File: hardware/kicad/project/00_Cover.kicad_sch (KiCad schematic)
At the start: 0 parts

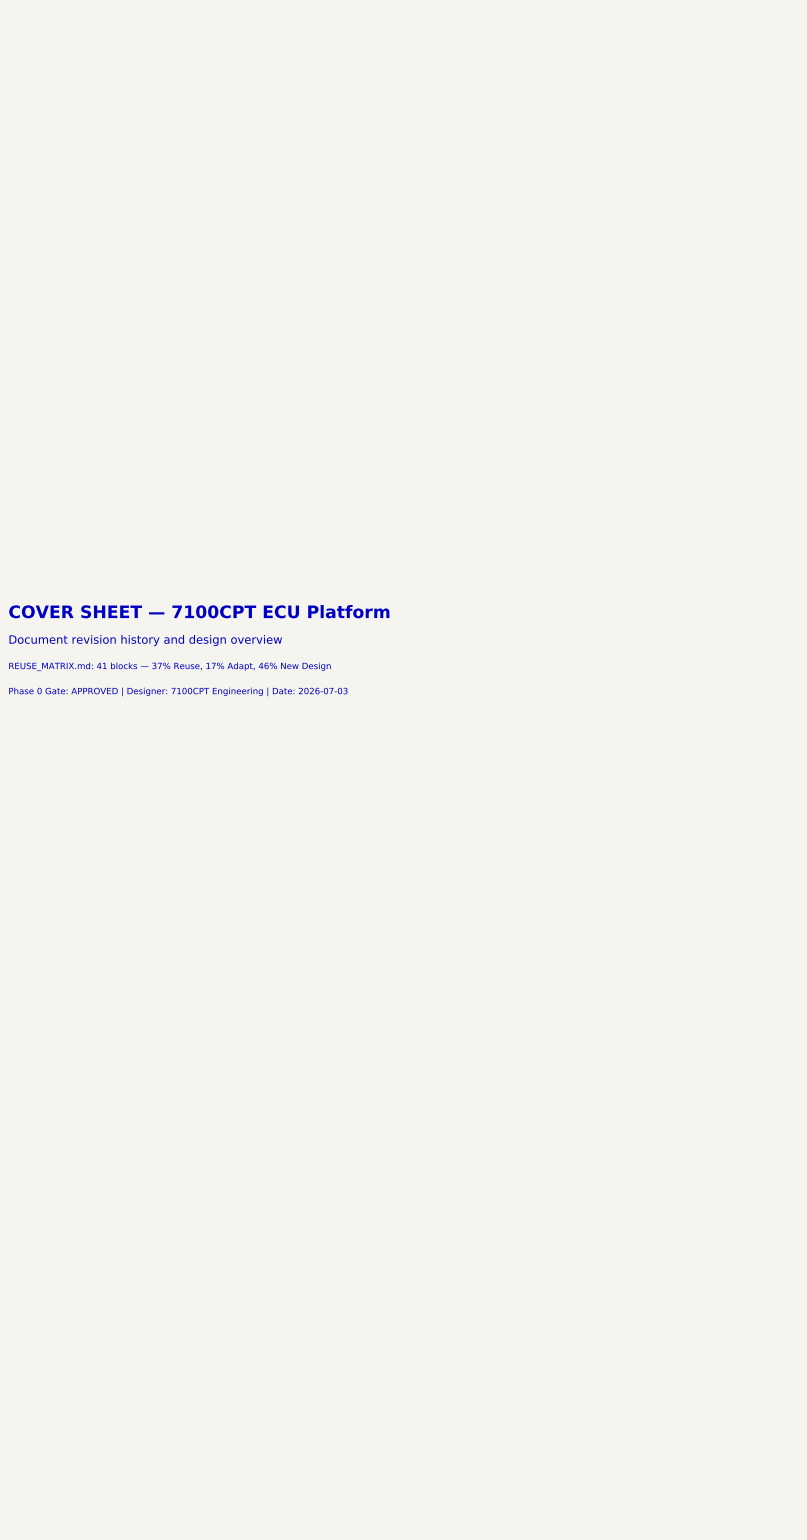
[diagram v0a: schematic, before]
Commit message: feat(hardware): TB-HW-002 — populate all 12 schematic sheets with components
Populated 235 component symbols across all 12 KiCad schematic sheets:
- 01_Power: Reverse polarity, TVS (SMCJ33A), buck (LMR33630), LDO (TPS7A1633), VREF (REF5050) — 30 symbols
- 02_MCU: S32K344 (6 units), clock (40MHz+32kHz), decoupling, reset, boot config, LEDs — 30 symbols
- 03_CAN: 4x TJA1043 with CM chokes (ACT45B-510), split termination, bus filter caps — 36 symbols
- 04_USB: Molex USB-C, TPD2EUSB30 ESD, CC resistors, eFuse, Ethernet PHY footprint — 9 symbols
- 05_Inputs: 8 analog channels (RC+clamp), 2x CJ125 WBO2, 2x TLE2072 knock amps — 50 symbols
- 06_Injectors: TLE8888-2QK (8-ch P&H), flyback diodes, current sense — 14 symbols
- 07_Ignition: 6x ISL9V3040S3 IGBTs with gate resistors (100R), pull-downs (10k) — 24 symbols
- 08_Outputs: DRV8873 ETC H-bridge, TLE8110ED low-side (boost+relays), BTS4140N tach — 12 symbols
- 09_Protection: TPS3850G33 watchdog, safe-state FET, ESD diodes (PESD5V0) — 14 symbols
- 10_Connectors: 42-pin Deutsch DTM (2 units), 2x CAN 4-pin, diagnostic 4-pin — 5 symbols
- 11_Programming: TC2050 SWD, 8 test points, production security notes — 11 symbols
- 00_Cover: Block diagram, BOM summary, spec references, revision history

Symbol library: 18 custom symbols with complete pin assignments
Components from COMPONENT_SELECTION.md r0.1
42-pin connector per INTERFACE_SPECIFICATION.md (authority)
All MCU pins per MCU_SELECTION.md pin allocation
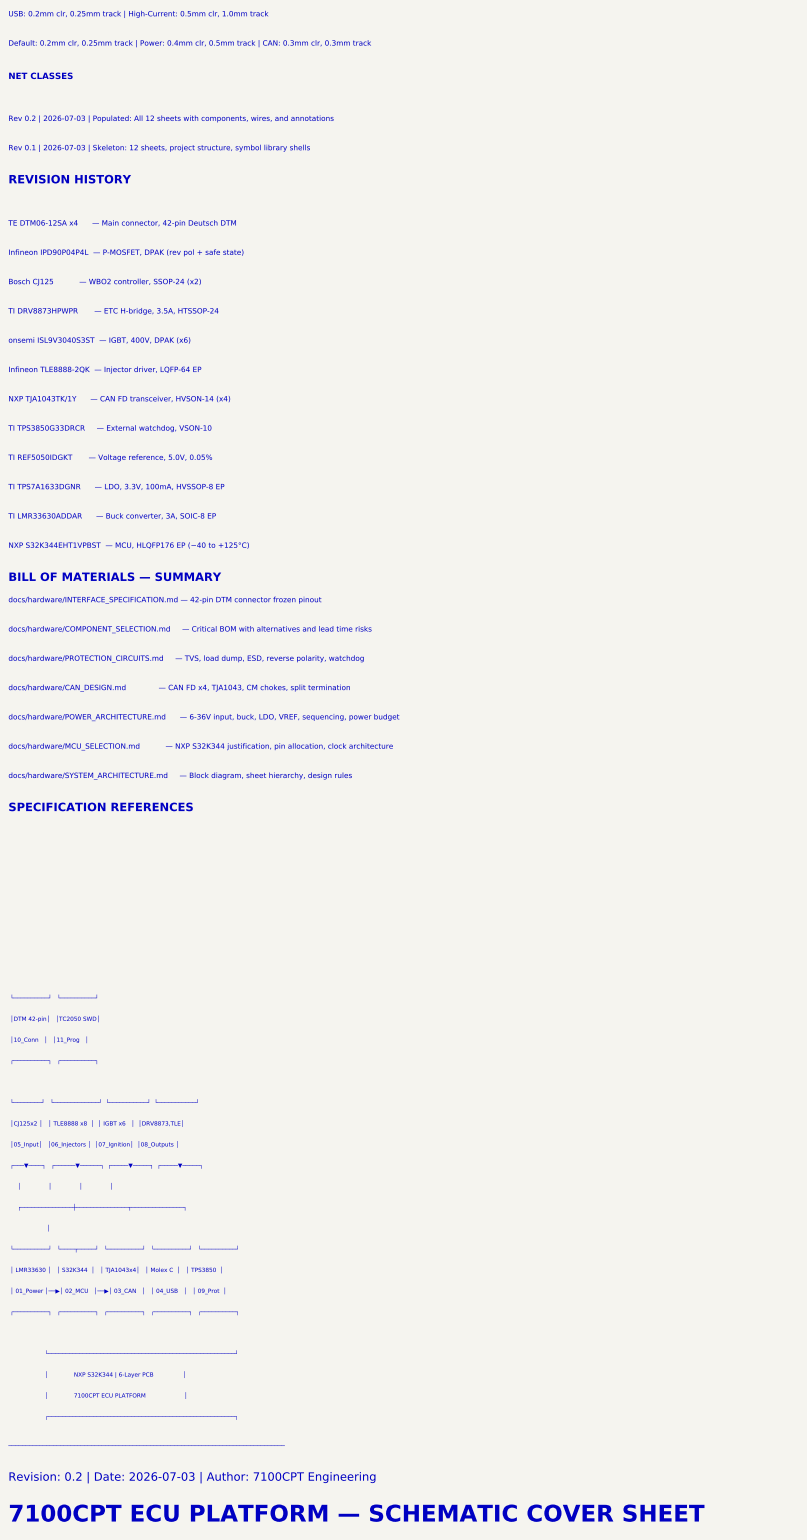
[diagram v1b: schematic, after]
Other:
- note added: "7100CPT ECU PLATFORM — SCHEMATIC COVER SHEET"
- note added: "BILL OF MATERIALS — SUMMARY"
- note added: "Bosch CJ125 — WBO2 controller, SSOP-24 (x2)"
- note added: "Default: 0.2mm clr, 0.25mm track | Power: 0.4mm clr, 0.5mm track | CAN: 0.3mm clr, 0.3mm track"
- note added: "Infineon IPD90P04P4L — P-MOSFET, DPAK (rev pol + safe state)"
- note added: "Infineon TLE8888-2QK — Injector driver, LQFP-64 EP"
- note added: "NET CLASSES"
- note added: "NXP S32K344EHT1VPBST — MCU, HLQFP176 EP (−40 to +125°C)"
- note added: "NXP TJA1043TK/1Y — CAN FD transceiver, HVSON-14 (x4)"
- note added: "REVISION HISTORY"
- note added: "Rev 0.1 | 2026-07-03 | Skeleton: 12 sheets, project structure, symbol library shells"
- note added: "Rev 0.2 | 2026-07-03 | Populated: All 12 sheets with components, wires, and annotations"
- note added: "Revision: 0.2 | Date: 2026-07-03 | Author: 7100CPT Engineering"
- note added: "SPECIFICATION REFERENCES"
- note added: "TE DTM06-12SA x4 — Main connector, 42-pin Deutsch DTM"
- note added: "TI DRV8873HPWPR — ETC H-bridge, 3.5A, HTSSOP-24"
- note added: "TI LMR33630ADDAR — Buck converter, 3A, SOIC-8 EP"
- note added: "TI REF5050IDGKT — Voltage reference, 5.0V, 0.05%"
- note added: "TI TPS3850G33DRCR — External watchdog, VSON-10"
- note added: "TI TPS7A1633DGNR — LDO, 3.3V, 100mA, HVSSOP-8 EP"
- note added: "USB: 0.2mm clr, 0.25mm track | High-Current: 0.5mm clr, 1.0mm track"
- note added: "docs/hardware/CAN_DESIGN.md — CAN FD x4, TJA1043, CM chokes, split termination"
- note added: "docs/hardware/COMPONENT_SELECTION.md — Critical BOM with alternatives and lead time risks"
- note added: "docs/hardware/INTERFACE_SPECIFICATION.md — 42-pin DTM connector frozen pinout"
- note added: "docs/hardware/MCU_SELECTION.md — NXP S32K344 justification, pin allocation, clock architecture"
- note added: "docs/hardware/POWER_ARCHITECTURE.md — 6-36V input, buck, LDO, VREF, sequencing, power budget"
- note added: "docs/hardware/PROTECTION_CIRCUITS.md — TVS, load dump, ESD, reverse polarity, watchdog"
- note added: "docs/hardware/SYSTEM_ARCHITECTURE.md — Block diagram, sheet hierarchy, design rules"
- note added: "onsemi ISL9V3040S3ST — IGBT, 400V, DPAK (x6)"
- note added: "────────────────────────────────────────────────────────────────────────────────"
- note added: "│"
- note added: "│ 01_Power │──▶│ 02_MCU │──▶│ 03_CAN │ │ 04_USB │ │ 09_Prot │"
- note added: "│ 7100CPT ECU PLATFORM │"
- note added: "│ LMR33630 │ │ S32K344 │ │ TJA1043x4│ │ Molex C │ │ TPS3850 │"
- note added: "│ NXP S32K344 | 6-Layer PCB │"
- note added: "│ │ │ │"
- note added: "│05_Input│ │06_Injectors │ │07_Ignition│ │08_Outputs │"
- note added: "│10_Conn │ │11_Prog │"
- note added: "│CJ125x2 │ │ TLE8888 x8 │ │ IGBT x6 │ │DRV8873,TLE│"
- note added: "│DTM 42-pin│ │TC2050 SWD│"
- note added: "┌──────────────────────────────────────────────────────┐"
- note added: "┌───────────────┼───────────────┬───────────────┐"
- note added: "┌──────────┐ ┌──────────┐"
- note added: "┌──────────┐ ┌──────────┐ ┌──────────┐ ┌──────────┐ ┌──────────┐"
- note added: "┌───▼────┐ ┌──────▼──────┐ ┌─────▼─────┐ ┌─────▼─────┐"
- note added: "└──────────────────────────────────────────────────────┘"
- note added: "└──────────┘ └──────────┘"
- note added: "└──────────┘ └────┬─────┘ └──────────┘ └──────────┘ └──────────┘"
- note added: "└────────┘ └─────────────┘ └───────────┘ └───────────┘"
- note removed: "COVER SHEET — 7100CPT ECU Platform"
- note removed: "Document revision history and design overview"
- note removed: "Phase 0 Gate: APPROVED | Designer: 7100CPT Engineering | Date: 2026-07-03"
- note removed: "REUSE_MATRIX.md: 41 blocks — 37% Reuse, 17% Adapt, 46% New Design"
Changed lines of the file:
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@@
-(kicad_sch (version 20240108) (generator "eeschema")
+(kicad_sch (version 20240108) (generator "7100CPT-schematic-gen")
   (paper "A3")
   (title_block
     (title "7100CPT ECU — Cover & Revision History")
     (date "2026-07-03")
-    (rev "0.1")
+    (rev "0.2")
     (company "${COMPANY}")
-    (comment 1 "Revision history, block diagram, BOM summary, REUSE_MATRIX reference")
+    (comment 1 "Cover sheet, block diagram, BOM summary, REUSE_MATRIX reference")
     (comment 2 "NXP S32K344 | rusEFI Firmware | IPC Class 3")
     (comment 3 "High-Tg FR-4 (TG170+) | ENIG | 1.6 mm")
-    (comment 4 "REUSE_MATRIX.md — NXP Reference Following")
+    (comment 4 "Phase 0 Approved | REUSE_MATRIX gate passed")
     (comment 5 "-40C to +85C | IP67 Target | 6-Layer")
   )
   (symbol_instances)
-  (text "COVER SHEET — 7100CPT ECU Platform"
-    (at 25 24 0) (effects (font (size 3.0 3.0) bold) (justify left bottom)))
-  (text "Document revision history and design overview"
-    (at 25 30 0) (effects (font (size 2.0 2.0)) (justify left bottom)))
-  (text "REUSE_MATRIX.md: 41 blocks — 37% Reuse, 17% Adapt, 46% New Design"
-    (at 25 36 0) (effects (font (size 1.5 1.5)) (justify left bottom)))
-  (text "Phase 0 Gate: APPROVED | Designer: 7100CPT Engineering | Date: 2026-07-03"
-    (at 25 42 0) (effects (font (size 1.5 1.5)) (justify left bottom)))
+  (text "7100CPT ECU PLATFORM — SCHEMATIC COVER SHEET" (at 25 240 0) (effects (font (size 4.0 4.0) bold) (justify left bottom)))
+  (text "Revision: 0.2 | Date: 2026-07-03 | Author: 7100CPT Engineering" (at 25 230 0) (effects (font (size 2.0 2.0)) (justify left bottom)))
+  (text "────────────────────────────────────────────────────────────────────────────────" (at 25 222 0) (effects (font (size 1.0 1.0)) (justify left bottom)))
+  (text "                    ┌──────────────────────────────────────────────────────┐" (at 25 215 0) (effects (font (size 1.0 1.0)) (justify left bottom)))
+  (text "                    │              7100CPT ECU PLATFORM                     │" (at 25 210 0) (effects (font (size 1.0 1.0)) (justify left bottom)))
+  (text "                    │              NXP S32K344 | 6-Layer PCB                │" (at 25 205 0) (effects (font (size 1.0 1.0)) (justify left bottom)))
+  (text "                    └──────────────────────────────────────────────────────┘" (at 25 200 0) (effects (font (size 1.0 1.0)) (justify left bottom)))
+  (text "" (at 25 195 0) (effects (font (size 1.0 1.0)) (justify left bottom)))
+  (text " ┌──────────┐   ┌──────────┐   ┌──────────┐   ┌──────────┐   ┌──────────┐" (at 25 190 0) (effects (font (size 1.0 1.0)) (justify left bottom)))
+  (text " │ 01_Power │──▶│ 02_MCU   │──▶│ 03_CAN   │   │ 04_USB   │   │ 09_Prot  │" (at 25 185 0) (effects (font (size 1.0 1.0)) (justify left bottom)))
+  (text " │ LMR33630 │   │ S32K344  │   │ TJA1043x4│   │ Molex C  │   │ TPS3850  │" (at 25 180 0) (effects (font (size 1.0 1.0)) (justify left bottom)))
+  (text " └──────────┘   └────┬─────┘   └──────────┘   └──────────┘   └──────────┘" (at 25 175 0) (effects (font (size 1.0 1.0)) (justify left bottom)))
+  (text "                     │" (at 25 170 0) (effects (font (size 1.0 1.0)) (justify left bottom)))
+  (text "     ┌───────────────┼───────────────┬───────────────┐" (at 25 165 0) (effects (font (size 1.0 1.0)) (justify left bottom)))
+  (text "     │               │               │               │" (at 25 160 0) (effects (font (size 1.0 1.0)) (justify left bottom)))
+  (text " ┌───▼────┐   ┌──────▼──────┐  ┌─────▼─────┐  ┌─────▼─────┐" (at 25 155 0) (effects (font (size 1.0 1.0)) (justify left bottom)))
+  (text " │05_Input│   │06_Injectors │  │07_Ignition│  │08_Outputs │" (at 25 150 0) (effects (font (size 1.0 1.0)) (justify left bottom)))
+  (text " │CJ125x2 │   │ TLE8888 x8  │  │ IGBT x6   │  │DRV8873,TLE│" (at 25 145 0) (effects (font (size 1.0 1.0)) (justify left bottom)))
+  (text " └────────┘   └─────────────┘  └───────────┘  └───────────┘" (at 25 140 0) (effects (font (size 1.0 1.0)) (justify left bottom)))
+  (text "" (at 25 135 0) (effects (font (size 1.0 1.0)) (justify left bottom)))
+  (text " ┌──────────┐   ┌──────────┐" (at 25 130 0) (effects (font (size 1.0 1.0)) (justify left bottom)))
+  (text " │10_Conn   │   │11_Prog   │" (at 25 125 0) (effects (font (size 1.0 1.0)) (justify left bottom)))
+  (text " │DTM 42-pin│   │TC2050 SWD│" (at 25 120 0) (effects (font (size 1.0 1.0)) (justify left bottom)))
+  (text " └──────────┘   └──────────┘" (at 25 115 0) (effects (font (size 1.0 1.0)) (justify left bottom)))
+  (text "SPECIFICATION REFERENCES" (at 25 70 0) (effects (font (size 2.0 2.0) bold) (justify left bottom)))
+  (text "docs/hardware/SYSTEM_ARCHITECTURE.md     — Block diagram, sheet hierarchy, design rules" (at 25 62 0) (effects (font (size 1.27 1.27)) (justify left bottom)))
+  (text "docs/hardware/MCU_SELECTION.md           — NXP S32K344 justification, pin allocation, clock architecture" (at 25 55 0) (effects (font (size 1.27 1.27)) (justify left bottom)))
+  (text "docs/hardware/POWER_ARCHITECTURE.md      — 6-36V input, buck, LDO, VREF, sequencing, power budget" (at 25 48 0) (effects (font (size 1.27 1.27)) (justify left bottom)))
+  (text "docs/hardware/CAN_DESIGN.md              — CAN FD x4, TJA1043, CM chokes, split termination" (at 25 41 0) (effects (font (size 1.27 1.27)) (justify left bottom)))
+  (text "docs/hardware/PROTECTION_CIRCUITS.md     — TVS, load dump, ESD, reverse polarity, watchdog" (at 25 34 0) (effects (font (size 1.27 1.27)) (justify left bottom)))
+  (text "docs/hardware/COMPONENT_SELECTION.md     — Critical BOM with alternatives and lead time risks" (at 25 27 0) (effects (font (size 1.27 1.27)) (justify left bottom)))
+  (text "docs/hardware/INTERFACE_SPECIFICATION.md — 42-pin DTM connector frozen pinout" (at 25 20 0) (effects (font (size 1.27 1.27)) (justify left bottom)))
+  (text "BILL OF MATERIALS — SUMMARY" (at 25 15 0) (effects (font (size 2.0 2.0) bold) (justify left bottom)))
+  (text "NXP S32K344EHT1VPBST  — MCU, HLQFP176 EP (−40 to +125°C)" (at 25 7 0) (effects (font (size 1.27 1.27)) (justify left bottom)))
+  (text "TI LMR33630ADDAR      — Buck converter, 3A, SOIC-8 EP" (at 25 0 0) (effects (font (size 1.27 1.27)) (justify left bottom)))
+  (text "TI TPS7A1633DGNR      — LDO, 3.3V, 100mA, HVSSOP-8 EP" (at 25 -7 0) (effects (font (size 1.27 1.27)) (justify left bottom)))
+  (text "TI REF5050IDGKT       — Voltage reference, 5.0V, 0.05%" (at 25 -14 0) (effects (font (size 1.27 1.27)) (justify left bottom)))
+  (text "TI TPS3850G33DRCR     — External watchdog, VSON-10" (at 25 -21 0) (effects (font (size 1.27 1.27)) (justify left bottom)))
+  (text "NXP TJA1043TK/1Y      — CAN FD transceiver, HVSON-14 (x4)" (at 25 -28 0) (effects (font (size 1.27 1.27)) (justify left bottom)))
+  (text "Infineon TLE8888-2QK  — Injector driver, LQFP-64 EP" (at 25 -35 0) (effects (font (size 1.27 1.27)) (justify left bottom)))
+  (text "onsemi ISL9V3040S3ST  — IGBT, 400V, DPAK (x6)" (at 25 -42 0) (effects (font (size 1.27 1.27)) (justify left bottom)))
+  (text "TI DRV8873HPWPR       — ETC H-bridge, 3.5A, HTSSOP-24" (at 25 -49 0) (effects (font (size 1.27 1.27)) (justify left bottom)))
+  (text "Bosch CJ125           — WBO2 controller, SSOP-24 (x2)" (at 25 -56 0) (effects (font (size 1.27 1.27)) (justify left bottom)))
+  (text "Infineon IPD90P04P4L  — P-MOSFET, DPAK (rev pol + safe state)" (at 25 -63 0) (effects (font (size 1.27 1.27)) (justify left bottom)))
+  (text "TE DTM06-12SA x4      — Main connector, 42-pin Deutsch DTM" (at 25 -70 0) (effects (font (size 1.27 1.27)) (justify left bottom)))
+  (text "REVISION HISTORY" (at 25 -80 0) (effects (font (size 2.0 2.0) bold) (justify left bottom)))
+  (text "Rev 0.1 | 2026-07-03 | Skeleton: 12 sheets, project structure, symbol library shells" (at 25 -88 0) (effects (font (size 1.27 1.27)) (justify left bottom)))
+  (text "Rev 0.2 | 2026-07-03 | Populated: All 12 sheets with components, wires, and annotations" (at 25 -95 0) (effects (font (size 1.27 1.27)) (justify left bottom)))
+  (text "NET CLASSES" (at 25 -105 0) (effects (font (size 1.5 1.5) bold) (justify left bottom)))
+  (text "Default: 0.2mm clr, 0.25mm track | Power: 0.4mm clr, 0.5mm track | CAN: 0.3mm clr, 0.3mm track" (at 25 -113 0) (effects (font (size 1.27 1.27)) (justify left bottom)))
+  (text "USB: 0.2mm clr, 0.25mm track | High-Current: 0.5mm clr, 1.0mm track" (at 25 -120 0) (effects (font (size 1.27 1.27)) (justify left bottom)))
   (sheet_instances
     (path "/00_cover/" (page "1"))
